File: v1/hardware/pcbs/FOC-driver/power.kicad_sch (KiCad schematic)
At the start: 32 parts, among them J1 HB9500M-9.5-2P, Q7 SP015N03BGHTO

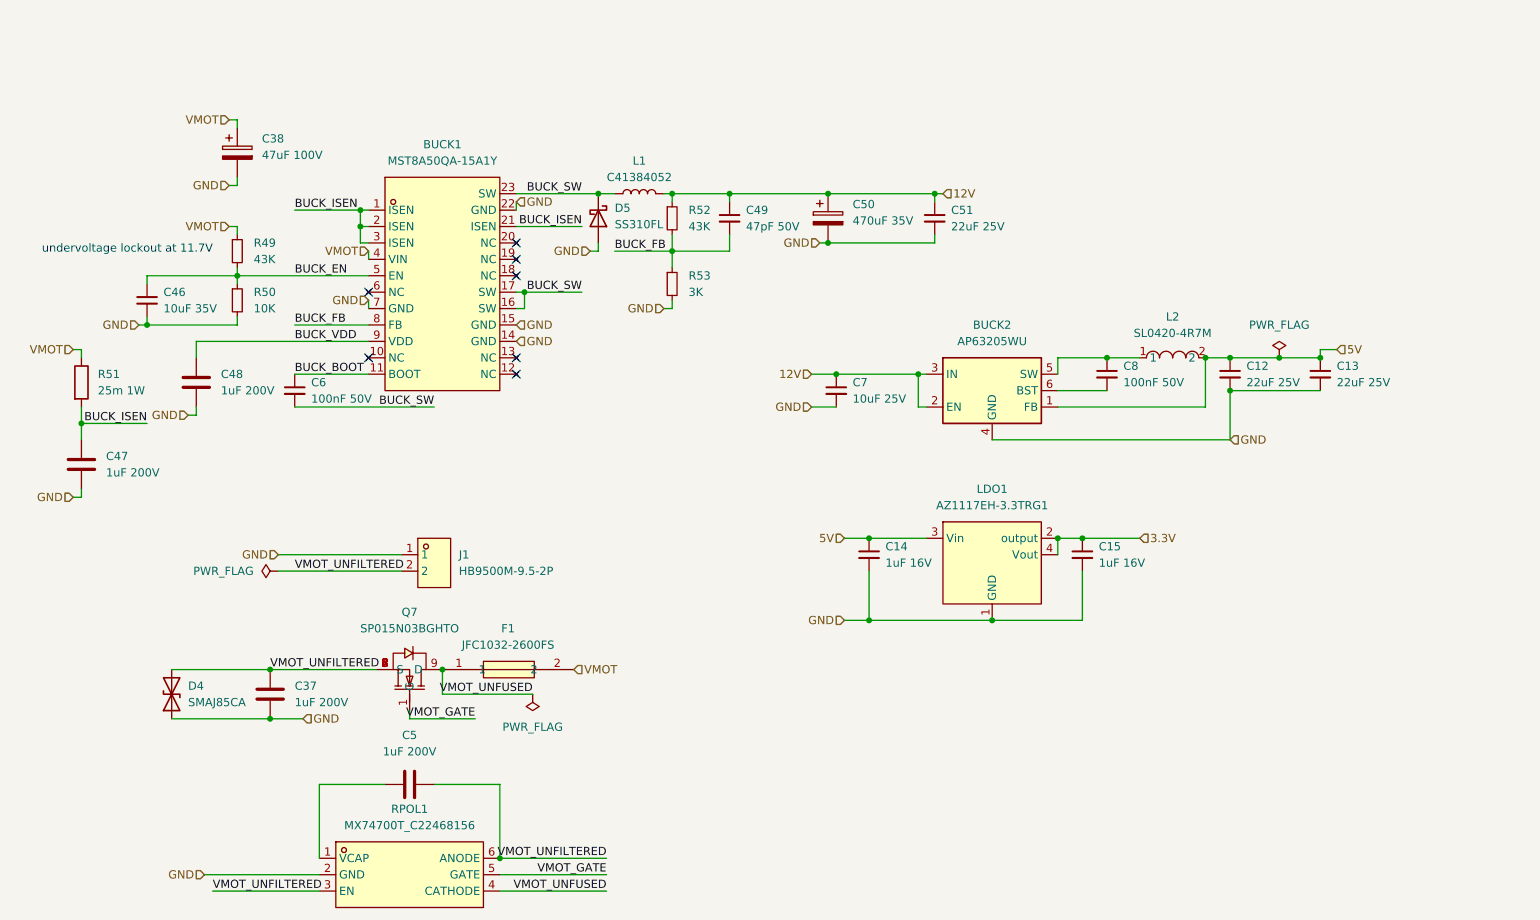
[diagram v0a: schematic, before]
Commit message: new FOC driver power step-down layout and inverter layout
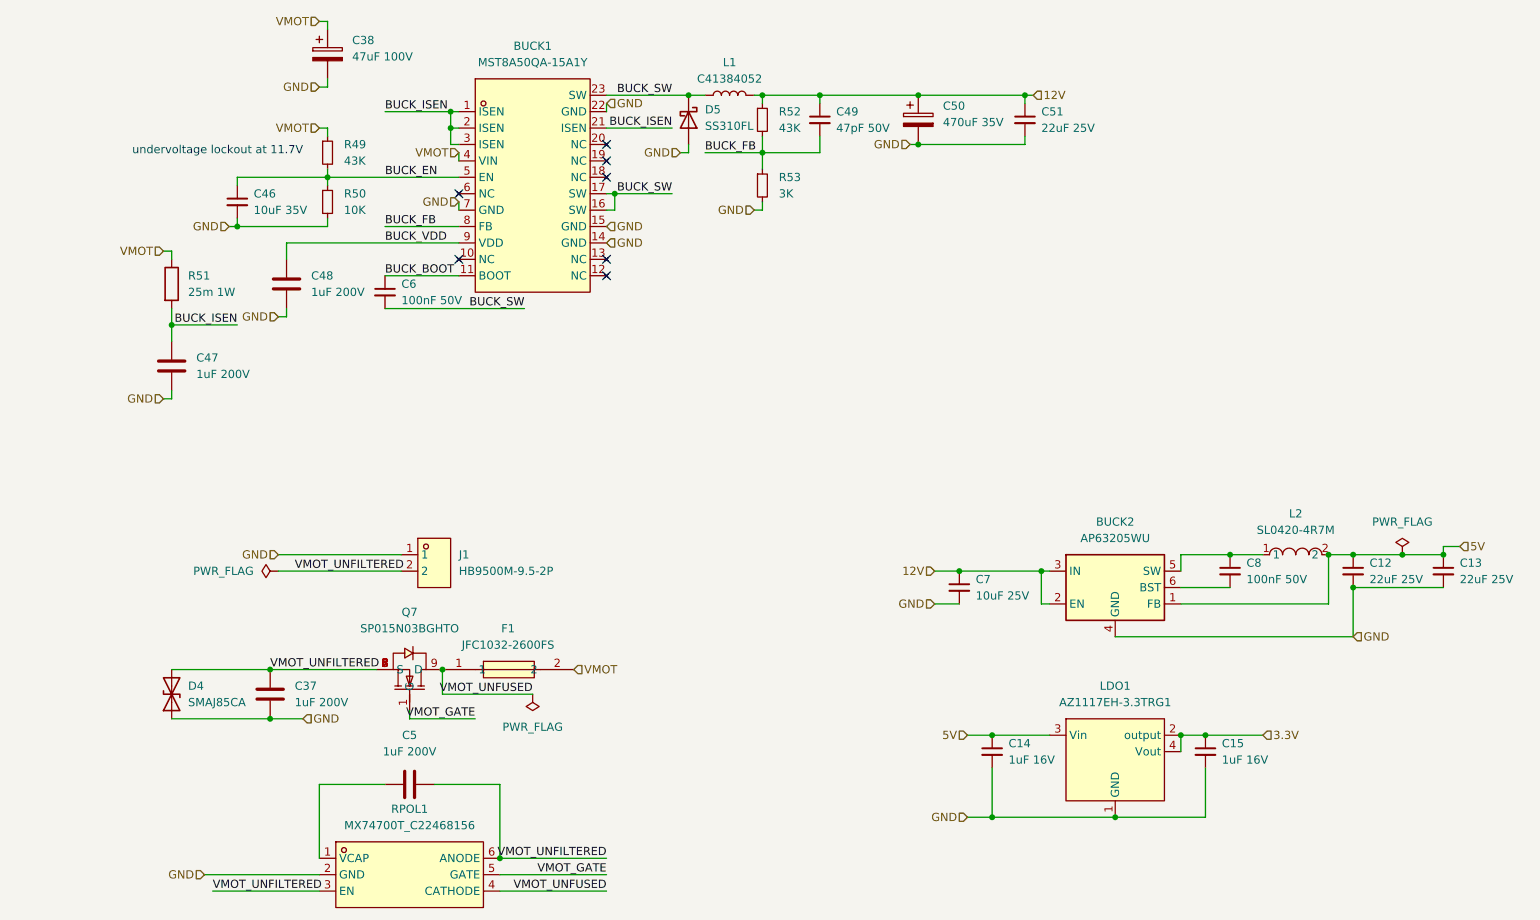
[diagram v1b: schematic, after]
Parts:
- R52: footprint Resistor_SMD:R_0805_2012Metric -> footprints:R_0805_2012Metric
- R53: footprint Resistor_SMD:R_0805_2012Metric -> Resistor_SMD:R_0402_1005Metric
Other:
- moved on the sheet: BUCK1, BUCK2, C12, C13, C14, C15, C38, C46, C47, C48, C49, C50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

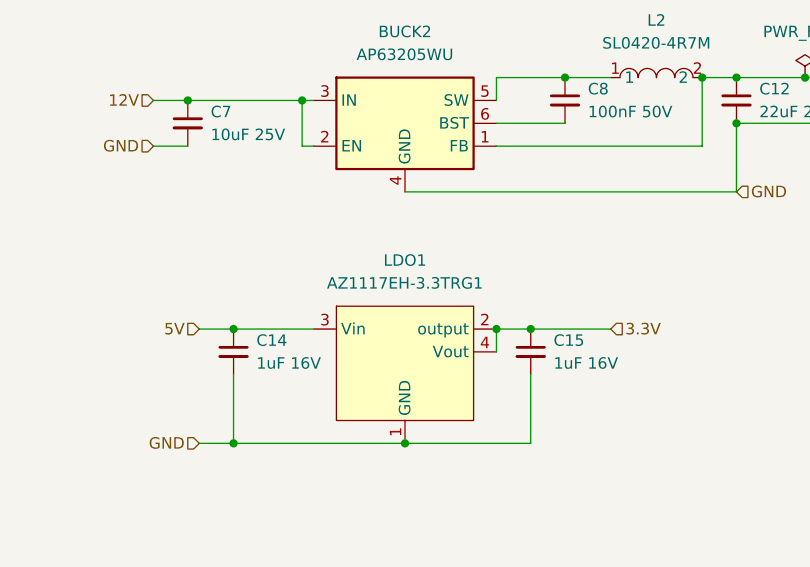
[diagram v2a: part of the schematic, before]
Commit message: replaced 3.3V LDO with AZ1117CH-3.3TRG1, + production files
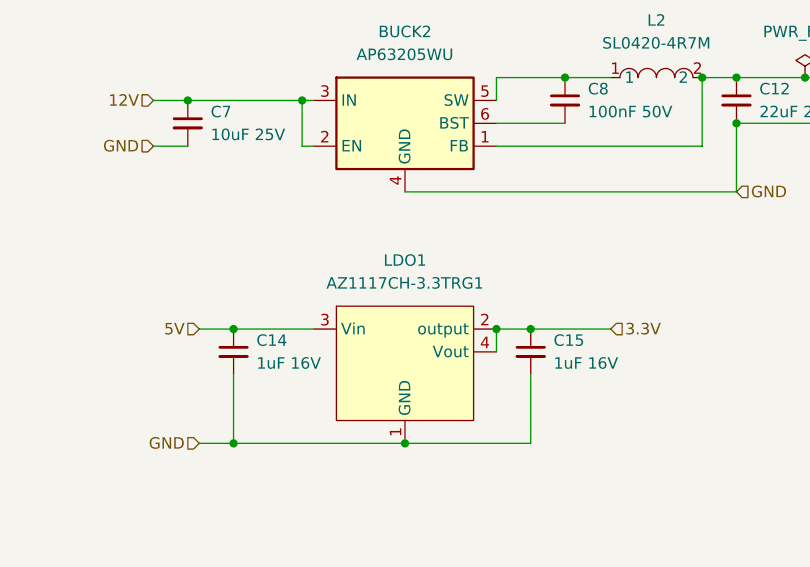
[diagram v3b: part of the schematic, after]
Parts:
- LDO1: value AZ1117EH-3.3TRG1 -> AZ1117CH-3.3TRG1
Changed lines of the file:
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@@
 			)
 		)
-		(property "Value" "AZ1117EH-3.3TRG1"
+		(property "Value" "AZ1117CH-3.3TRG1"
 			(at 198.12 140.97 0)
 			(effects
@@
 			)
 		)
-		(property "Datasheet" "https://lcsc.com/product-detail/Low-Dropout-Regulators-LDO_DIODES_AZ1117EH-3-3TRG1_AZ1117EH-3-3TRG1_C108494.html"
+		(property "Datasheet" "https://lcsc.com/datasheet/lcsc_datasheet_2412251154_DIODES-AZ1117CH-3-3TRG1_C92102.pdf"
 			(at 198.12 168.91 0)
 			(effects
